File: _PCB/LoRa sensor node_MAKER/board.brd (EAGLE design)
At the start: 53.3 x 78.2 mm, 25 parts

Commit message: CH340E converter complete + LoRa sensor node
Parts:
- removed MICRO_1, MICRO_2, MICRO_3: (no value), SparkFun-Connectors:USB-MICROB
- added USB1, USB2, USB3: ST-USB-001G, Seeed-Connector:MICRO-USB5+4P-SMD-0.65-B
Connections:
- net 5V: now also USB1.5, USB2.5, USB3.5; no longer MICRO_1.VBUS, MICRO_2.VBUS, MICRO_3.VBUS
- net GND: now also USB1.1, USB1.S1, USB1.S2, USB1.S3, USB1.S4, USB1.S5, USB1.S6, USB2.1, USB2.S1, USB2.S2, USB2.S3, USB2.S4, USB2.S5, USB2.S6, USB3.1, USB3.S1, USB3.S2, USB3.S3, USB3.S4, USB3.S5, USB3.S6; no longer MICRO_1.GND, MICRO_2.GND, MICRO_3.GND
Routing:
- net 5V: track 145.8 -> 149.6 mm

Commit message: error correciton
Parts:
- removed USB1: ST-USB-001G, Seeed-Connector:MICRO-USB5+4P-SMD-0.65-B
- moved BME280_1-3 5.80 mm to (9.40, 26.2), turned to 180 degrees
- moved BME280_4-6 5.33 mm to (4.32, 16.0)
- moved C9 2.79 mm to (8.89, 21.6)
- moved USB2 2.54 mm to (43.9, -5.08)
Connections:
- net 5V: no longer USB1.5
- net GND: no longer USB1.1, USB1.S1, USB1.S2, USB1.S3, USB1.S4, USB1.S5, USB1.S6
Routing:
- net 5V: track 149.6 -> 131.0 mm
- net SDA: track 33.9 -> 39.2 mm
- net SCL: track 19.4 -> 24.2 mm
- net 3.3V: track 113.7 -> 113.0 mm

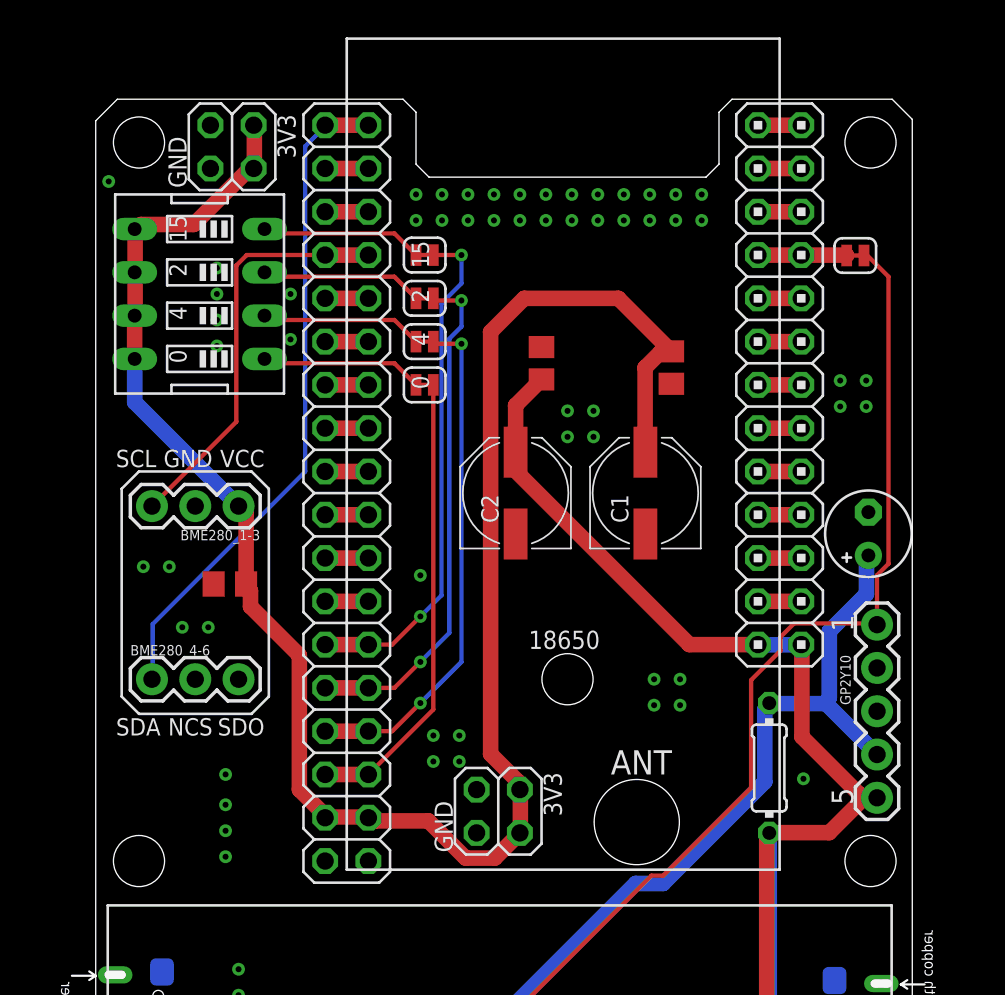
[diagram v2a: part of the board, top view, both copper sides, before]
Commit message: LoRa sensor node PCB update
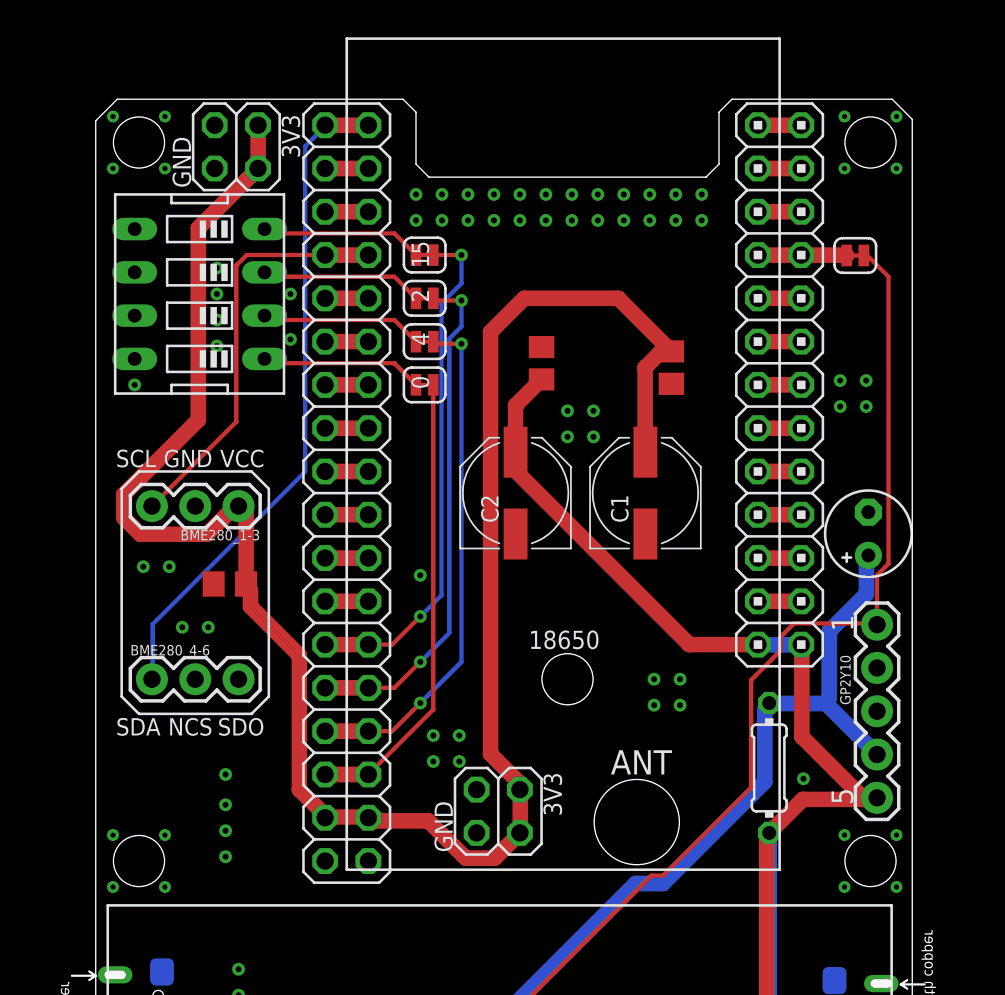
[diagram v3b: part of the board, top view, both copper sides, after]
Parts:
- moved JP8 0.25 mm to (9.27, 47.2)
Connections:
- net 3.3V: no longer SW1.5, SW1.6, SW1.7, SW1.8
- net GND: now also SW1.5, SW1.6, SW1.7, SW1.8
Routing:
- net 3.3V: track 113.0 -> 117.3 mm
- net GND: vias 74 -> 90
